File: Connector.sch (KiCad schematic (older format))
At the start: 11 parts, among them CON11 DISCO-CON1, CON21 DISCO-CON2

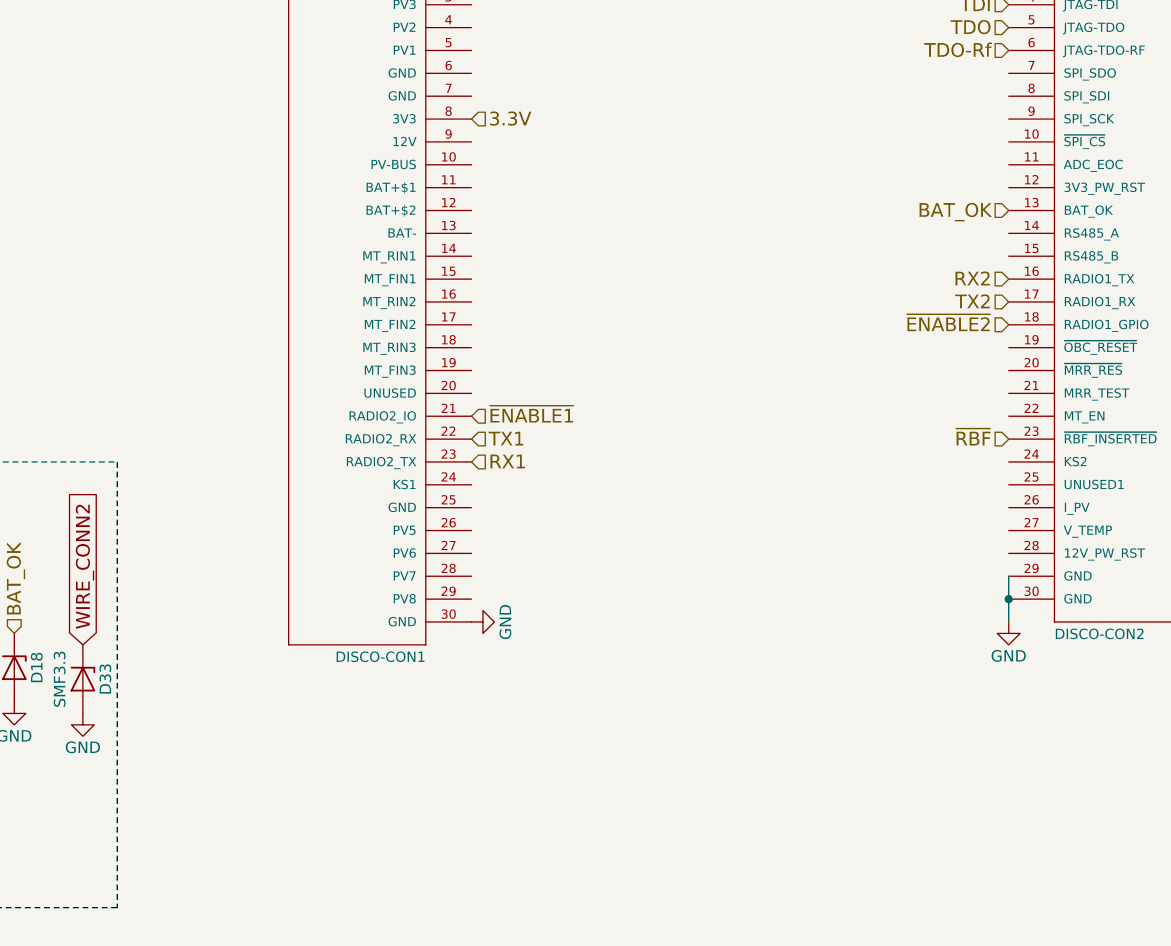
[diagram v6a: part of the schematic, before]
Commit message: Adds SMA and Burnwire connectors
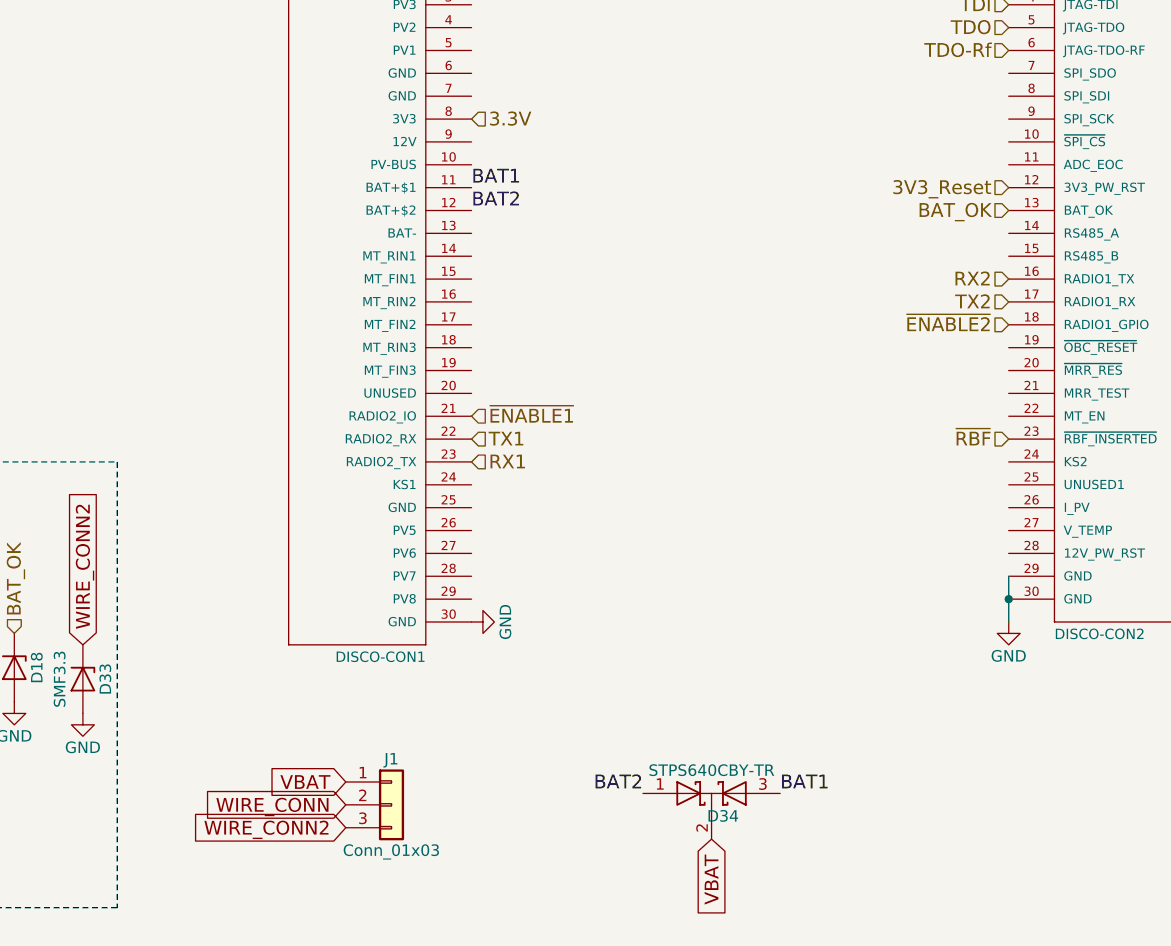
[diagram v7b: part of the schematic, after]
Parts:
- added D34: STPS640CBY-TR, TO_SOT_Packages_SMD:TO-252-2, symbol D_Schottky_x2_KCom_AKA
- added J1: Conn_01x03, Pin_Headers:Pin_Header_Straight_1x03_Pitch2.54mm, symbol Conn_01x03
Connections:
- net WIRE_CONN: now also J1.2 (Pin_2)
- net WIRE_CONN2: now also J1.3 (Pin_3)
- net 3V3_Reset: now reaches CON21.12 (3V3_PW_RST)
- net BAT1: now reaches CON11.11 (BAT+$1)
- net BAT1: now also D34.3 (A)
- net BAT2: now reaches CON11.12 (BAT+$2)
- net BAT2: now also D34.1 (A)
- new net VBAT: D34.2 (K), J1.1 (Pin_1)
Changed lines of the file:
@@
 LIBS:contrib
 LIBS:valves
-LIBS:nxp-ic
-LIBS:7400-ic
 LIBS:cubesatFunkmodul-cache
 LIBS:funkmodul
-LIBS:CubeSat-Bus-1
-LIBS:CubeSat-Bus-2
 LIBS:disco-con
 EELAYER 25 0
@@
 	1    0    0    -1
 $EndComp
+$Comp
+L Conn_01x03 J1
+U 1 1 5A0DBE27
+P 6750 5100
+F 0 "J1" H 6750 5300 50  0000 C CNN
+F 1 "Conn_01x03" H 6750 4900 50  0000 C CNN
+F 2 "Pin_Headers:Pin_Header_Straight_1x03_Pitch2.54mm" H 6750 5100 50  0001 C CNN
+F 3 "" H 6750 5100 50  0001 C CNN
+	1    6750 5100
+	1    0    0    -1
+$EndComp
+Text HLabel 9450 2400 0    60   Input ~ 0
+3V3_Reset
+Text GLabel 6550 5000 0    60   Input ~ 0
+VBAT
+Text GLabel 6550 5100 0    60   Input ~ 0
+WIRE_CONN
+Text GLabel 6550 5200 0    60   Input ~ 0
+WIRE_CONN2
+Text Label 7100 2400 0    60   ~ 0
+BAT1
+Text Label 7100 2500 0    60   ~ 0
+BAT2
+$Comp
+L D_Schottky_x2_KCom_AKA D34
+U 1 1 5A0DCFFC
+P 8150 5050
+F 0 "D34" H 8200 4950 50  0000 C CNN
+F 1 "STPS640CBY-TR" H 8150 5150 50  0000 C CNN
+F 2 "TO_SOT_Packages_SMD:TO-252-2" H 8150 5050 50  0001 C CNN
+F 3 "http://www.st.com/content/ccc/resource/technical/document/datasheet/bd/b7/a5/a5/2a/bc/4e/65/DM00091810.pdf/files/DM00091810.pdf/jcr:content/translations/en.DM00091810.pdf" H 8150 5050 50  0001 C CNN
+	1    8150 5050
+	1    0    0    -1
+$EndComp
+Text GLabel 8150 5250 3    60   Input ~ 0
+VBAT
+Text Label 8450 5050 0    60   ~ 0
+BAT1
+Text Label 7850 5050 2    60   ~ 0
+BAT2
 $EndSCHEMATC

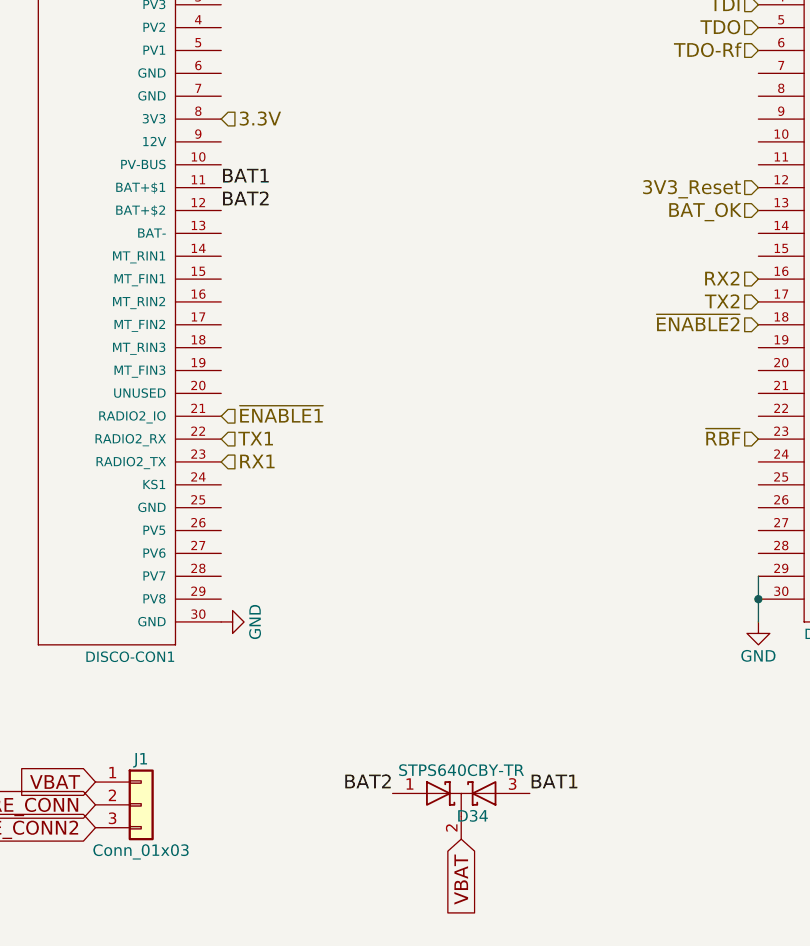
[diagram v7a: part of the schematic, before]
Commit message: Adds stiching vias
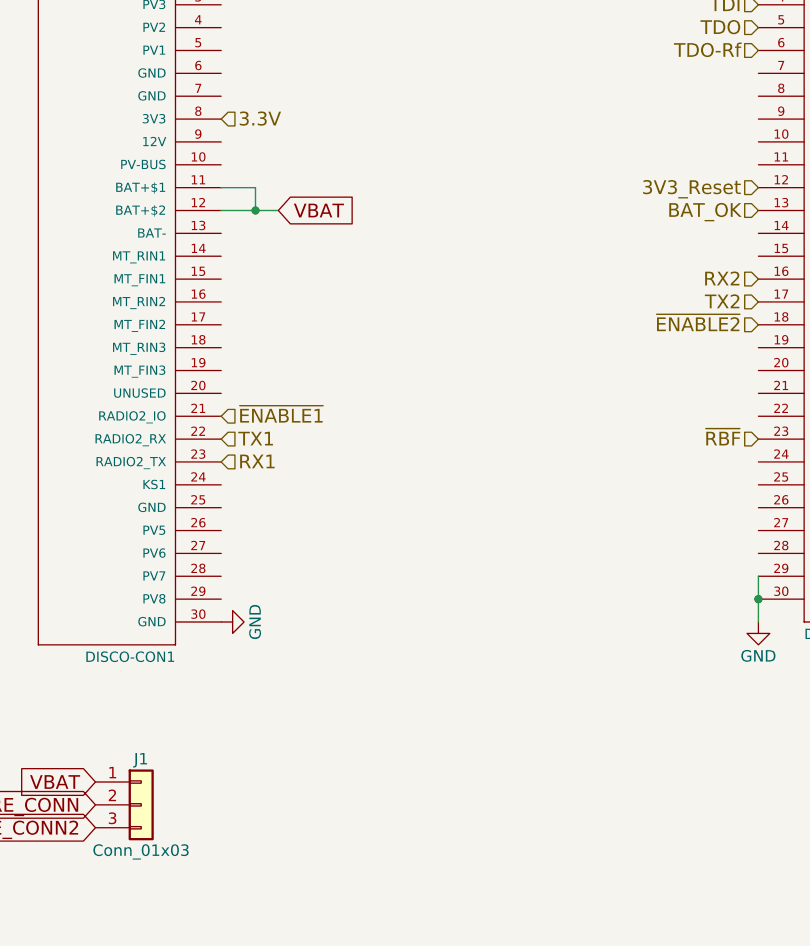
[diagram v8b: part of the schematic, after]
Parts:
- removed D34: STPS640CBY-TR, TO_SOT_Packages_SMD:TO-252-2, symbol D_Schottky_x2_KCom_AKA
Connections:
- net BAT1 is gone; now on net VBAT: CON11.11 (BAT+$1)
- net BAT2 is gone; now on net VBAT: CON11.12 (BAT+$2)
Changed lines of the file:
@@
 LIBS:contrib
 LIBS:valves
+LIBS:nxp-ic
+LIBS:7400-ic
 LIBS:cubesatFunkmodul-cache
 LIBS:funkmodul
+LIBS:CubeSat-Bus-1
+LIBS:CubeSat-Bus-2
 LIBS:disco-con
 EELAYER 25 0
@@
 Text GLabel 6550 5200 0    60   Input ~ 0
 WIRE_CONN2
-Text Label 7100 2400 0    60   ~ 0
-BAT1
-Text Label 7100 2500 0    60   ~ 0
-BAT2
-$Comp
-L D_Schottky_x2_KCom_AKA D34
-U 1 1 5A0DCFFC
-P 8150 5050
-F 0 "D34" H 8200 4950 50  0000 C CNN
-F 1 "STPS640CBY-TR" H 8150 5150 50  0000 C CNN
-F 2 "TO_SOT_Packages_SMD:TO-252-2" H 8150 5050 50  0001 C CNN
-F 3 "http://www.st.com/content/ccc/resource/technical/document/datasheet/bd/b7/a5/a5/2a/bc/4e/65/DM00091810.pdf/files/DM00091810.pdf/jcr:content/translations/en.DM00091810.pdf" H 8150 5050 50  0001 C CNN
-	1    8150 5050
-	1    0    0    -1
-$EndComp
-Text GLabel 8150 5250 3    60   Input ~ 0
+Wire Wire Line
+	7100 2400 7250 2400
+Wire Wire Line
+	7100 2500 7350 2500
+Wire Wire Line
+	7250 2400 7250 2500
+Connection ~ 7250 2500
+Text GLabel 7350 2500 2    60   Input ~ 0
 VBAT
-Text Label 8450 5050 0    60   ~ 0
-BAT1
-Text Label 7850 5050 2    60   ~ 0
-BAT2
 $EndSCHEMATC
